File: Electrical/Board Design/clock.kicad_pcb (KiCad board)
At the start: 2 copper layers, 133.3 x 50.8 mm, 40 parts, among them CON1 AVR-ISP-6, IC1 ATTINY84A-SS, Q1 FET_N, Q2 FET_P, SW1 SPST, U1 MCP1624, X1 CRYSTAL 32.768kHz

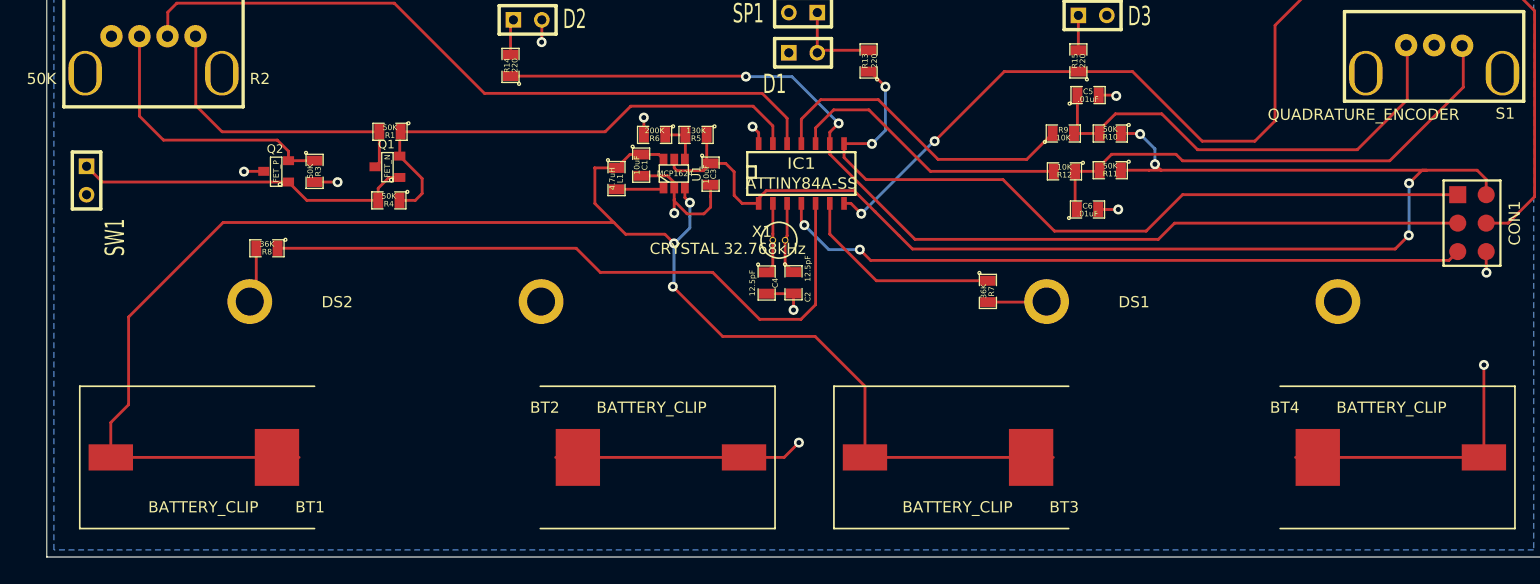
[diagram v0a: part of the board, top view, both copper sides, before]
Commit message: added LDO to schematic and board
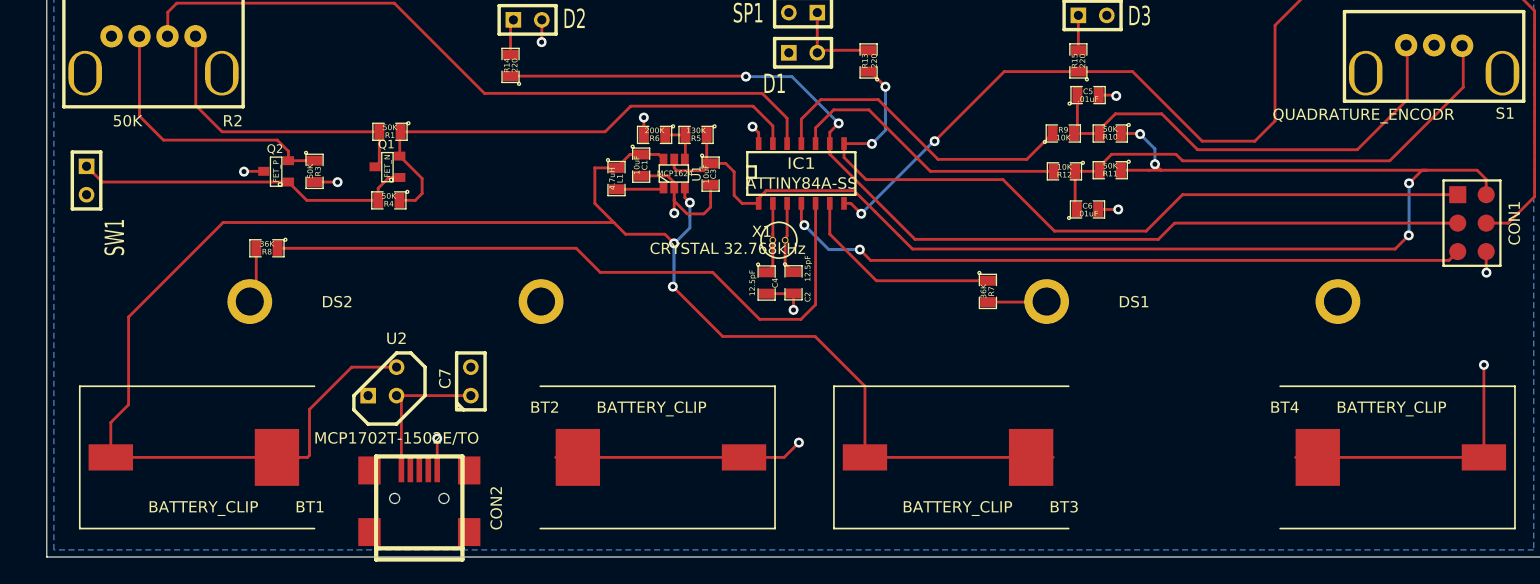
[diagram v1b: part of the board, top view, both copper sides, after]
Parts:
- added C7: 1uF, C1, F.Cu at (171.2, 214.2)
- added CON2: USB-MICRO-B, USB_MINI_B, F.Cu at (166.6, 225.5)
- added U2: MCP1702T-1502E/TO, TO92, F.Cu at (163.3, 214.2)
- S1: value QUADRATURE_ENCODER -> QUADRATURE_ENCODR
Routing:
- net N-0000011: track 149.0 -> 163.4 mm
- net N-0000020: track 0.00 -> 13.4 mm
- net GND: track 77.7 -> 80.4 mm, vias 12 -> 13

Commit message: electrical design updates
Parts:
- added P1: CONN_6, SIL-6, F.Cu at (234.6, 226.9)
- added P2: , SIL-2, F.Cu at (247.7, 226.9)
- added P3: , SIL-2, F.Cu at (254.3, 226.9)
- BT1, BT2, BT3, BT4: footprint AA_battery_clip_single -> AA_Battery_Clip_THRU_HOLE_BK-92
- R1, R3, R4: value 50K -> 100K
- R2: value 50K -> 100K; moved to B.Cu
- S1: value QUADRATURE_ENCODR -> QUADRATURE_ENCODER; moved to B.Cu
- U2: footprint TO92 -> TO92-INVERT
- X1: footprint CRYSTAL -> SMD_CRYSTAL_SMALL
- moved Q1 20.7 mm to (143.1, 193.1), turned to 0 degrees
- moved R4 20.5 mm to (143.4, 196.8)
- moved R1 17.2 mm to (147.0, 194.9), turned to 90 degrees
- moved C7 11.9 mm to (159.4, 212.7), turned to 180 degrees
- moved DS1 5.12 mm to (227.7, 207.0)
- moved DS2 5.04 mm to (146.4, 207.0)
- moved BT2 4.70 mm to (183.4, 218.4)
- moved BT4 4.09 mm to (250.2, 218.4)
- moved U2 3.75 mm to (167.0, 214.8), turned to 90 degrees
- moved BT1 3.62 mm to (149.8, 218.4)
- moved BT3 3.28 mm to (216.7, 218.4)
- moved Q2 3.22 mm to (151.1, 193.8)
- moved R3 3.22 mm to (154.5, 193.8)
- moved C5 1.05 mm to (226.2, 189.7)
- turned R2 to 0 degrees
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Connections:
- BT1 pad ~: N-0000011 (its old number) -> /BATTERY POWER
- BT3 pad ~: N-0000011 (its old number) -> /BATTERY POWER
- C1 pad 1: N-0000011 (its old number) -> /BATTERY POWER
- DS1 pad 1: N-0000030 (its old number) -> /HOURS
- DS2 pad 1: N-0000029 (its old number) -> /MINUTES
- L1 pad 1: N-0000011 (its old number) -> /BATTERY POWER
- R7 pad 2: N-0000030 (its old number) -> /HOURS
- R8 pad 2: N-0000029 (its old number) -> /MINUTES
- U1 pad 3: N-0000011 (its old number) -> /BATTERY POWER
- U1 pad 6: N-0000011 (its old number) -> /BATTERY POWER
- U2 pad 3: N-0000011 (its old number) -> /BATTERY POWER
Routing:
- net /BATTERY POWER: track 0.00 -> 180.8 mm, vias 0 -> 3
- net N-0000011 (its old number): track 163.4 -> 0.00 mm, vias 3 -> 0
- net /MINUTES: track 0.00 -> 104.9 mm
- net /MODE SELECT: track 64.3 -> 161.6 mm, vias 0 -> 4
- net VCC: track 122.3 -> 179.6 mm, vias 4 -> 6
- net /HOURS: track 0.00 -> 37.9 mm
- net GND: track 80.4 -> 46.9 mm, vias 13 -> 11
- net /MODE SELECT POWER: track 45.1 -> 67.0 mm, vias 0 -> 2
- net /AM PM LIGHT: track 102.5 -> 88.6 mm
- net N-000004: track 26.6 -> 15.2 mm
- net /INT 2: track 28.5 -> 38.9 mm
- net /INT 1: track 25.6 -> 35.8 mm
- net N-0000010: track 30.7 -> 20.6 mm
- net N-000005: track 24.9 -> 16.7 mm
- net N-0000029 (its old number): track 5.00 -> 0.00 mm
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- added copper zone on F.Cu, net GND
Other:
- net class HEAVY added: clearance 0.254, trace_width 0.6, via_dia 0.889, via_drill 0.635
- board text added: "+"
- board text added: "+2.0V"
- board text added: "-"
- board text added: "AWK-105-005 Rev B"
- board text added: "GND"
- board text added: "HOURS"
- board text added: "MINUTES"
- board text added: "Thank you Kickstarter backers! - Sam"
- board text added: "www.awkwardengineer.com"

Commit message: board updates
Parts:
- P2, P3: value (none) -> CONN_2
- R1: value 100K -> 0K
- R10, R11: value 50K -> 130K
- R3: value 100K -> 10K
- R7, R8: value 36K -> 33K
- S1: value QUADRATURE_ENCODER -> QUADRATURE_ENCODR
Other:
- board text added: "AWK-105-005 Rev C"
- board text removed: "AWK-105-005 Rev B"
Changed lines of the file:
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@@
   (layers
     (15 F.Cu signal)
-    (0 B.Cu signal)
+    (0 B.Cu signal hide)
     (16 B.Adhes user)
     (17 F.Adhes user)
@@
       (effects (font (size 1 1) (thickness 0.15)) (justify mirror))
     )
-    (fp_text value QUADRATURE_ENCODER (at 0 3.804996) (layer B.SilkS)
+    (fp_text value QUADRATURE_ENCODR (at 0 3.804996) (layer B.SilkS)
       (effects (font (size 1 1) (thickness 0.15)) (justify mirror))
     )
@@
       (effects (font (size 0.50038 0.50038) (thickness 0.10922)))
     )
-    (fp_text value 36K (at -1.051 1.279 180) (layer F.SilkS)
+    (fp_text value 33K (at -1.051 1.279 180) (layer F.SilkS)
       (effects (font (size 0.50038 0.50038) (thickness 0.10922)))
     )
@@
       (effects (font (size 0.50038 0.50038) (thickness 0.10922)))
     )
-    (fp_text value 36K (at -0.811 1.323 270) (layer F.SilkS)
+    (fp_text value 33K (at -0.811 1.323 270) (layer F.SilkS)
       (effects (font (size 0.50038 0.50038) (thickness 0.10922)))
     )
@@
       (effects (font (size 0.50038 0.50038) (thickness 0.10922)))
     )
-    (fp_text value 100K (at 0.8382 1.2954 90) (layer F.SilkS)
+    (fp_text value 0K (at 0.8382 1.2954 90) (layer F.SilkS)
       (effects (font (size 0.50038 0.50038) (thickness 0.10922)))
     )
@@
       (effects (font (size 0.50038 0.50038) (thickness 0.10922)))
     )
-    (fp_text value 100K (at -0.8984 -1.347 270) (layer F.SilkS)
+    (fp_text value 10K (at -0.8984 -1.347 270) (layer F.SilkS)
       (effects (font (size 0.50038 0.50038) (thickness 0.10922)))
     )
@@
       (effects (font (size 0.50038 0.50038) (thickness 0.10922)))
     )
-    (fp_text value 50K (at -0.9652 -1.2192 180) (layer F.SilkS)
+    (fp_text value 130K (at -0.9652 -1.2192 180) (layer F.SilkS)
       (effects (font (size 0.50038 0.50038) (thickness 0.10922)))
     )
@@
       (effects (font (size 0.50038 0.50038) (thickness 0.10922)))
     )
-    (fp_text value 50K (at -0.9652 -1.3716 180) (layer F.SilkS)
+    (fp_text value 130K (at -0.9652 -1.3716 180) (layer F.SilkS)
       (effects (font (size 0.50038 0.50038) (thickness 0.10922)))
     )
@@
       (effects (font (size 1.72974 1.08712) (thickness 0.3048)))
     )
-    (fp_text value "" (at 2.667 -4.826) (layer F.SilkS) hide
+    (fp_text value CONN_2 (at 2.667 -4.826) (layer F.SilkS) hide
       (effects (font (size 1.524 1.016) (thickness 0.254)))
     )
@@
       (effects (font (size 1.72974 1.08712) (thickness 0.3048)))
     )
-    (fp_text value "" (at 0 -2.54) (layer F.SilkS) hide
+    (fp_text value CONN_2 (at 0 -2.54) (layer F.SilkS) hide
       (effects (font (size 1.524 1.016) (thickness 0.254)))
     )
@@
     (effects (font (size 3.048 3.048) (thickness 0.3)))
   )
-  (gr_text "AWK-105-005 Rev B" (at 146.9644 227.7364) (layer F.SilkS)
+  (gr_text "AWK-105-005 Rev C" (at 146.9644 227.7364) (layer F.SilkS)
     (effects (font (size 1.524 1.524) (thickness 0.3)))
   )

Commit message: release board design
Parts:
- added P4: , SIL-2, F.Cu at (80.4, 118.8)
- BT1, BT2, BT3, BT4: value BATTERY_CLIP -> (none)
- CON1: value AVR-ISP-6 -> (none); footprint pin_array_3x2 -> ISPheader
- CON2: value USB-MICRO-B -> (none); footprint USB_MINI_B -> USB_MINI_B_s
- P1: value CONN_6 -> (none); footprint SIL-6 -> SIL-6_s
- P2, P3: value CONN_2 -> (none)
- R10, R11: value 130K -> 51K
- moved BT3 130.0 mm to (141.2, 112.5)
- moved R1 130.0 mm to (71.6, 89.0)
- moved R10 130.0 mm to (152.8, 86.2)
- moved R11 130.0 mm to (152.8, 89.4)
- moved S1 130.0 mm to (181.7, 80.8)
- moved BT1 130.0 mm to (74.4, 112.5)
- moved BT2 130.0 mm to (108.0, 112.5)
- moved BT4 130.0 mm to (174.8, 112.5)
- moved C1 130.0 mm to (111.0, 89.0)
- moved C2 130.0 mm to (124.6, 99.5)
- moved C5 130.0 mm to (150.8, 83.8)
- moved CON1 130.0 mm to (185.1, 94.2)
- moved D1 130.0 mm to (125.4, 79.0)
- moved D3 130.0 mm to (151.3, 75.6)
- moved DS1 130.0 mm to (152.3, 101.1)
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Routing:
- net N-0000023: track 12.8 -> 25.5 mm
- net VCC: track 179.6 -> 183.4 mm
- net GND: track 46.9 -> 49.7 mm, vias 11 -> 12
- net /ALARM LIGHT: track 92.6 -> 93.9 mm
- net /MODE SELECT: track 161.6 -> 162.6 mm
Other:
- board text added: "+5v"

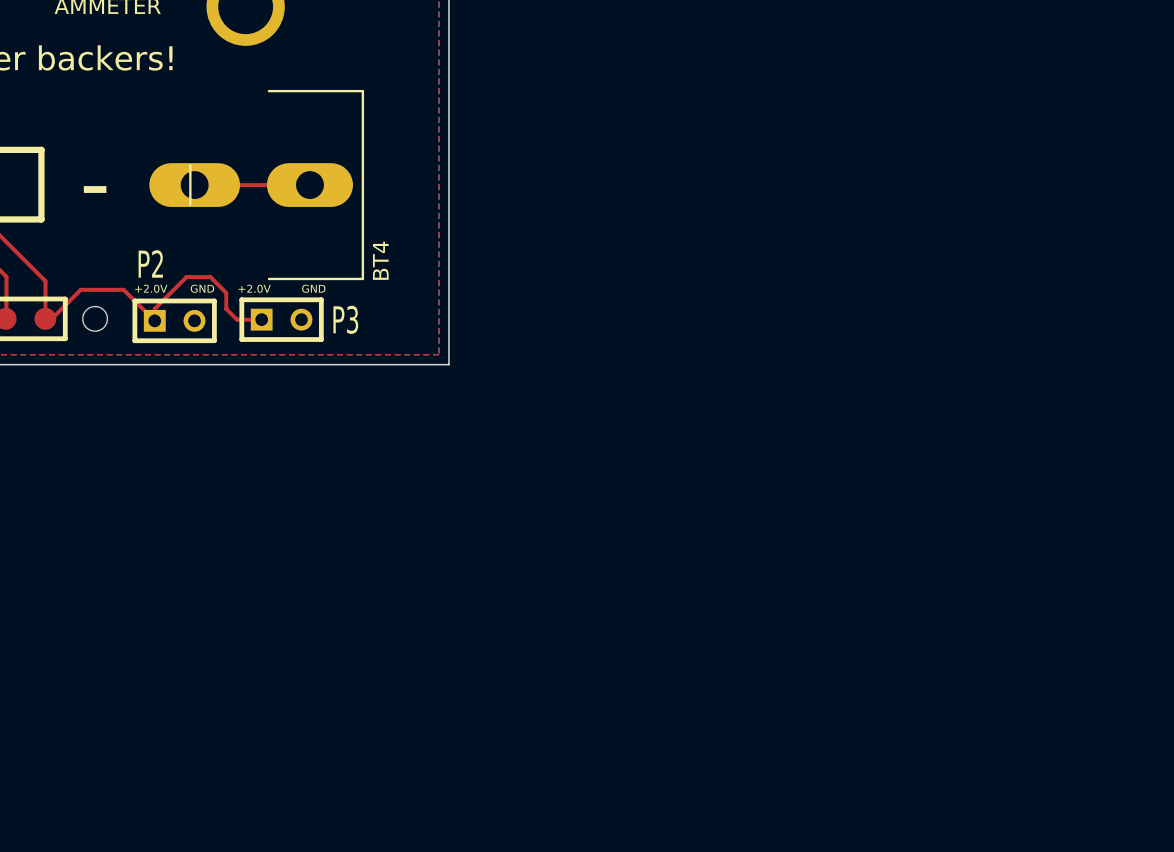
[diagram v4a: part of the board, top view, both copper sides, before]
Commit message: foot print and schematic updates
got the LED TE connector, SMT LDO, transistor for AM/PM lights
footprints and schematic updated
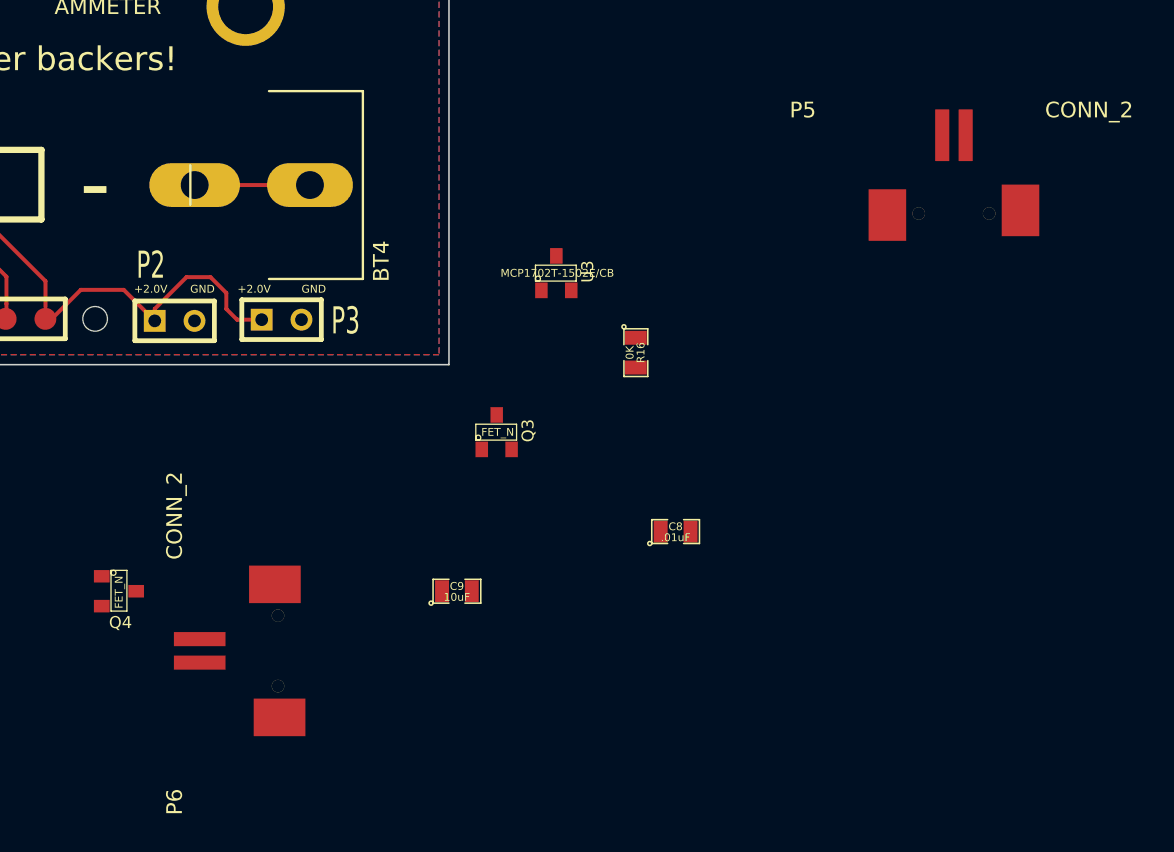
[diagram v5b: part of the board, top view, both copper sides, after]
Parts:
- added C8: .01uF, SM0805, F.Cu at (205.7, 134.6)
- added C9: 10uF, SM0805, F.Cu at (191.8, 138.4)
- added P5: CONN_2, TE-connectivity-2, F.Cu at (223.5, 114.3)
- added P6: CONN_2, TE-connectivity-2, F.Cu at (180.3, 142.2)
- added Q3: FET_N, SOT23, F.Cu at (194.3, 128.3)
- added Q4: FET_N, SOT23, F.Cu at (170.2, 138.4)
- added R16: 0K, SM0805, F.Cu at (203.2, 123.2)
- added U3: MCP1702T-1502E/CB, SOT23, F.Cu at (198.1, 118.1)
- BT1, BT2, BT3, BT4: value (none) -> BATTERY_CLIP
- CON1: value (none) -> AVR-ISP-6
- CON2: value (none) -> USB-MICRO-B
- P1: value (none) -> CONN_6
- P2, P3, P4: value (none) -> CONN_2
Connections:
- C7 pad 1: N-0000023 -> +5V
- CON2 pad 1: N-0000023 -> +5V
- D2 pad 2: GND -> N-0000029
- D3 pad 2: GND -> N-0000027
- P4 pad 1: N-0000023 -> +5V
- Q1 pad D: N-0000010 (its old number) -> N-0000025
- Q1 pad S: /MODE SELECT POWER -> GND
- Q2 pad D: GND -> N-0000026
- Q2 pad S: N-0000011 -> /MODE SELECT POWER
- R1 pad 2: N-0000010 (its old number) -> N-0000026
- R14 pad 1: /ALARM LIGHT -> +5V
- R15 pad 1: /AM PM LIGHT -> N-0000028
- R2 pad 1: N-0000010 (its old number) -> N-0000026
- R2 pad 3: N-0000011 -> N-0000025
- R3 pad 1: N-0000011 -> N-0000025
- U2 pad 2: N-0000023 -> +5V
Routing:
- net +5V: track 0.00 -> 56.0 mm, vias 0 -> 2
- net /ALARM LIGHT: track 93.9 -> 63.4 mm, vias 2 -> 0
- net N-0000023: track 25.5 -> 0.00 mm
- net N-0000028: track 0.00 -> 24.3 mm
- net /AM PM LIGHT: track 88.6 -> 64.2 mm
- net N-0000011: track 16.7 -> 0.00 mm
- net N-0000010 (its old number): track 15.2 -> 0.00 mm
- net N-0000025: track 0.00 -> 13.2 mm
- net /MODE SELECT POWER: track 67.0 -> 78.3 mm
- net N-0000026: track 0.00 -> 6.25 mm, vias 0 -> 1
- net N-0000029: track 0.00 -> 1.99 mm, vias 0 -> 1
- net GND: track 49.7 -> 48.9 mm, vias 12 -> 10

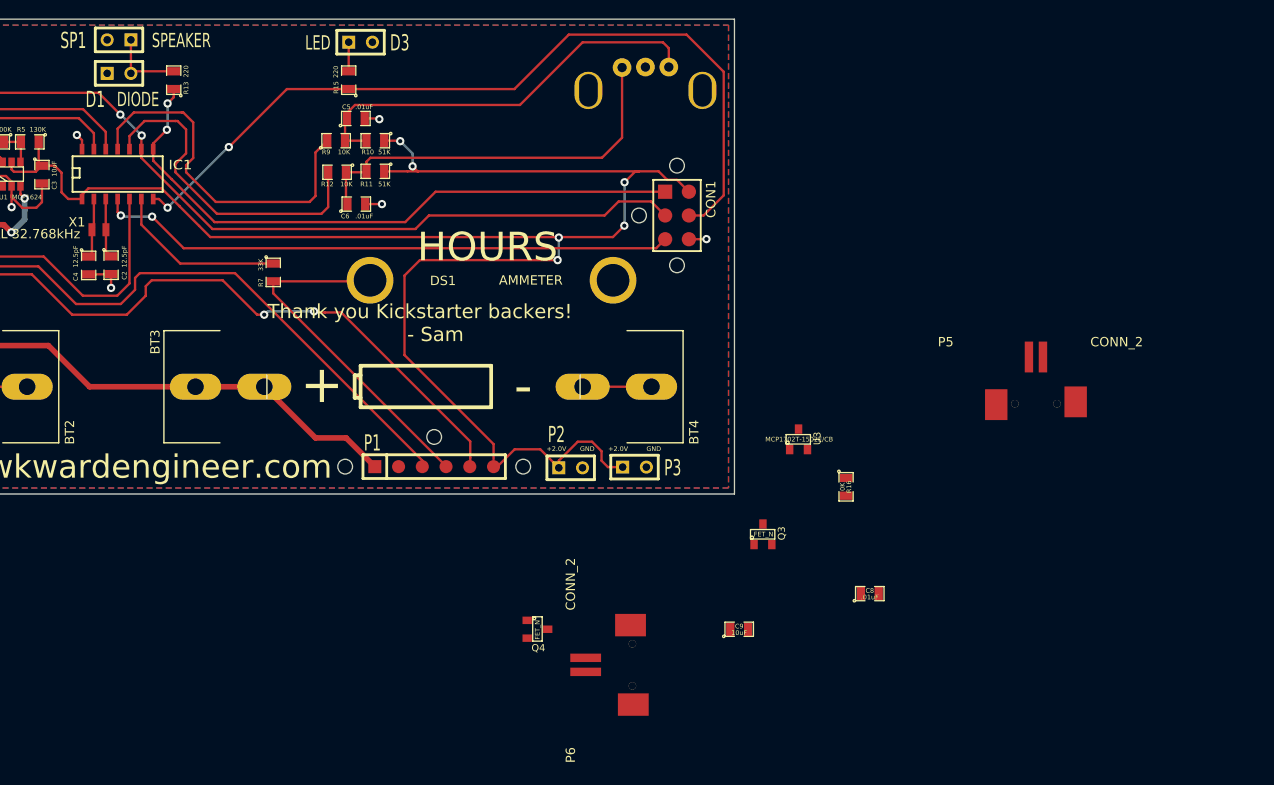
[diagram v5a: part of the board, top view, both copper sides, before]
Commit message: made changes to speaker footprint
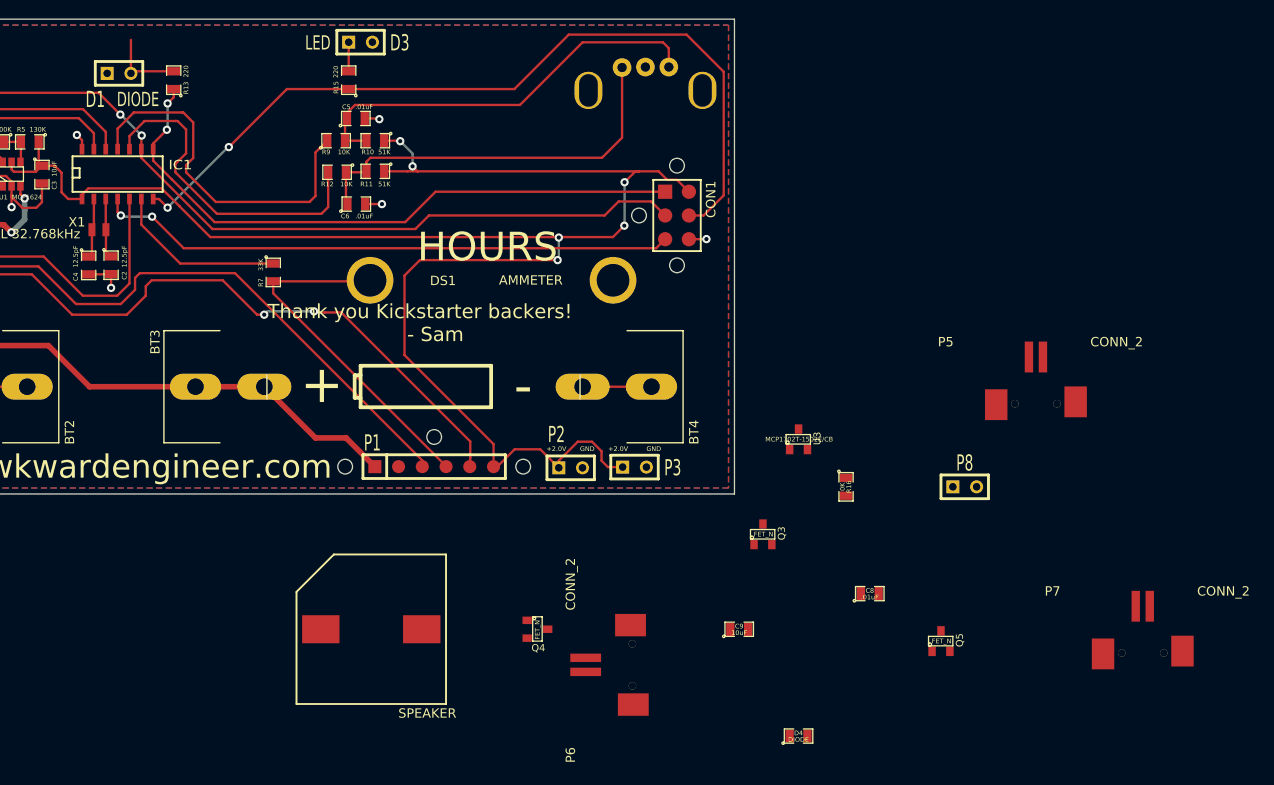
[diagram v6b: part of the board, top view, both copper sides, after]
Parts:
- added D4: DIODE, SM0805, F.Cu at (198.1, 149.9)
- added P7: CONN_2, TE-connectivity-2, F.Cu at (234.9, 141.0)
- added P8: CONN_2, SIL-2, F.Cu at (215.9, 123.2)
- added Q5: FET_N, SOT23, F.Cu at (213.4, 139.7)
- SP1: footprint SIL-2 -> SMT_BUZZER
- moved SP1 68.6 mm to (152.4, 138.4)
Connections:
- D1 pad 1: GND -> N-0000015
- D1 pad 2: N-000008 -> +5V
- R13 pad 1: /ALARM BUZZER -> +5V
- R13 pad 2: N-000008 -> N-0000015
- SP1 pad 1: N-000008 -> +5V
- SP1 pad 2: GND -> N-0000015
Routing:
- net +5V: track 56.0 -> 70.9 mm, vias 2 -> 4
- net N-000008: track 8.26 -> 0.00 mm
- net /ALARM BUZZER: track 67.4 -> 60.7 mm, vias 2 -> 0
- net N-0000018: track 13.2 -> 7.55 mm
- net N-0000016: track 6.25 -> 11.9 mm
